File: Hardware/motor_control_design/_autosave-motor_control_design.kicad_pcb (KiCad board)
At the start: 2 copper layers, 57.1 x 57.2 mm, 83 parts, among them J10 3V3, J2 SWD, J3 VBAT, J4 GND, J5 FC_M/P, J6 Conn_01x06, J8 Conn_01x06, J9 GND, Q1 RF1S9540SM, Q10 2N7002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

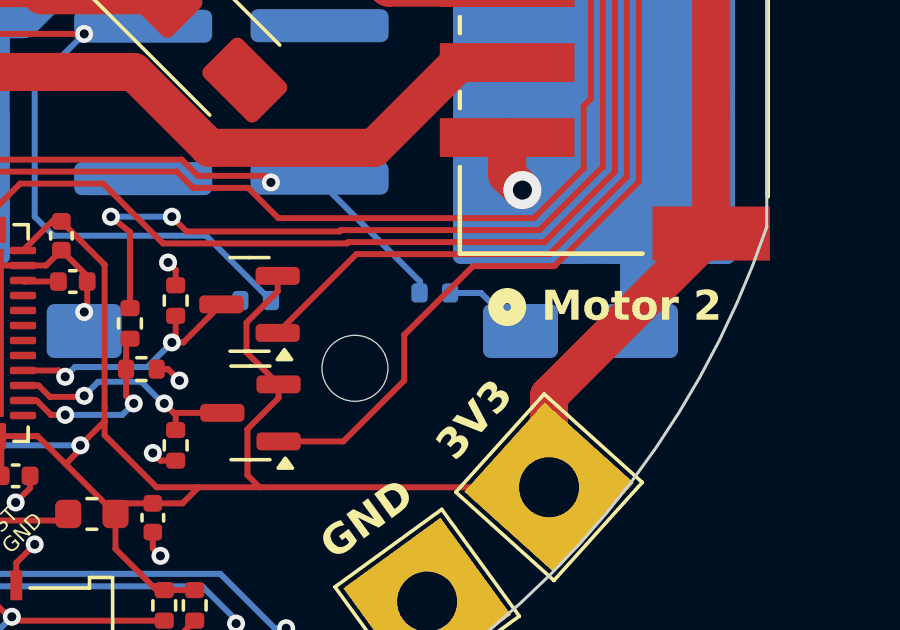
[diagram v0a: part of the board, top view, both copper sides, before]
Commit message: Updated Motor control schema and routing to match new hbridge design
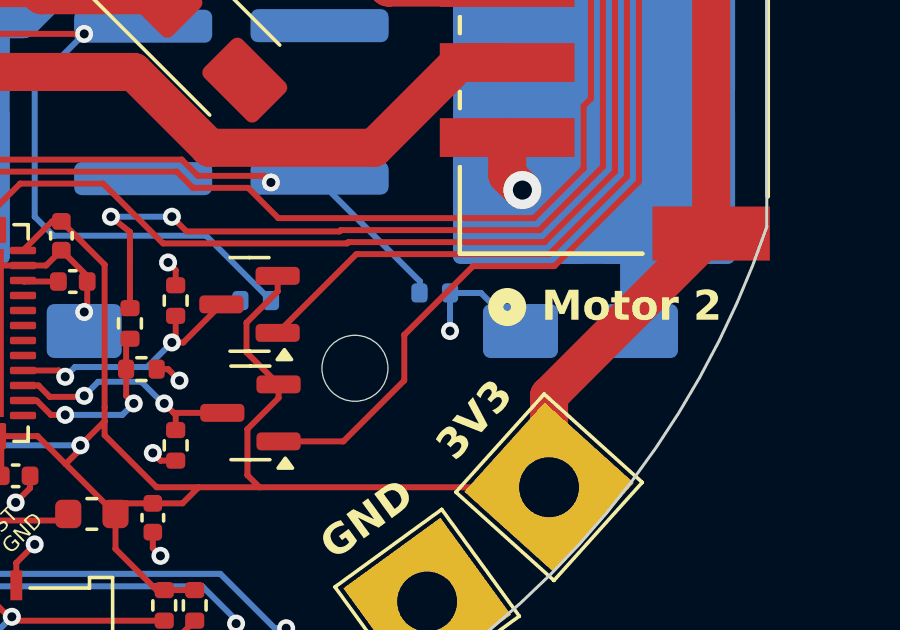
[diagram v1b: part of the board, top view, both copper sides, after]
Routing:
- net GND: track 193.2 -> 194.5 mm, vias 21 -> 22
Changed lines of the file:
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@@
+	)
+	(via
+		(at 167.005 102.362)
+		(size 0.6)
+		(drill 0.3)
+		(layers "F.Cu" "B.Cu")
+		(net 1)
 	)
 	(via
@@
 	)
 	(segment
+		(start 167.006999 101.092)
+		(end 167.005 102.362)
+		(width 0.2)
+		(layer "B.Cu")
+		(net 1)
+	)
+	(segment
 		(start 167.026998 101.092)
 		(end 168.039 101.092)
@@
 		(width 0.2)
 		(layer "B.Cu")
+		(net 1)
+	)
+	(segment
+		(start 167.005 102.362)
+		(end 167.006999 102.360001)
+		(width 0.2)
+		(layer "B.Cu")
